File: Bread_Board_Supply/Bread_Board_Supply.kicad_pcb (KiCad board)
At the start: 2 copper layers, 63 x 38.6 mm, 27 parts, among them J1 3.3_Connector, J2 5V_Connector, J3 12V_Connector, J4 Barrel_Jack_Switch, SW1 SW_Wuerth_450301014042, U1 TPS562202, U2 LP5907MFX-3.3

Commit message: Layout Changes
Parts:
- moved C1 8.39 mm to (141.4, 82.4)
- moved C8 8.20 mm to (114.1, 88.4), turned to 90 degrees
- moved BLM18AG102S1ND1 0.98 mm to (130.7, 80.5), turned to -90 degrees
- turned C9 to 90 degrees
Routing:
- net +3.3V: track 0.00 -> 25.6 mm
- net +5V: track 0.00 -> 8.50 mm
- net Net-(U1-VFB): track 0.00 -> 4.93 mm
- net Net-(U1-VBST): track 0.00 -> 4.72 mm, vias 0 -> 1
- net Net-(D3-A): track 0.00 -> 3.86 mm
- net Net-(D4-A): track 0.00 -> 2.58 mm
- net Net-(D2-A): track 0.00 -> 2.38 mm
- net Net-(U1-EN): track 0.00 -> 1.71 mm
- added copper zone on F.Cu, net +12V
- added copper zone on B.Cu, net GND
- added copper zone on F.Cu, net Net-(U1-EN)
- added copper zone on F.Cu, net Net-(U1-SW)

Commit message: Layout finished
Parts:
- moved R5 20.6 mm to (135.7, 93.1)
- moved BLM18AG102S1ND1 19.9 mm to (150.5, 79.4), turned to 90 degrees
- moved R4 15.1 mm to (123.0, 89.9)
- moved C7 14.2 mm to (133.6, 85.6)
- moved C2 8.70 mm to (140.2, 79.7)
- moved C9 6.05 mm to (114.1, 86.7), turned to 0 degrees
- moved C1 5.51 mm to (146.2, 79.7), turned to 90 degrees
- moved C6 4.86 mm to (127.8, 84.4)
- moved U1 4.77 mm to (126.4, 80.1)
- moved D2 4.65 mm to (132.8, 73.7)
- moved R3 4.65 mm to (149.1, 73.9)
- moved C8 4.14 mm to (114.1, 92.5)
- moved L1 3.99 mm to (122.3, 82.5)
- moved C10 2.74 mm to (134.4, 79.7), turned to 90 degrees
- moved J3 0.50 mm to (104.5, 101.5)
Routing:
- net +5V: track 8.50 -> 46.3 mm
- net +12V: track 0.00 -> 19.1 mm
- net Net-(U1-VFB): track 4.93 -> 17.9 mm
- net Net-(U1-SW): track 0.00 -> 9.10 mm
- net GND: track 0.00 -> 8.57 mm, vias 0 -> 1
- net Net-(U1-EN): track 1.71 -> 2.32 mm
- net Net-(U1-VBST): track 4.72 -> 4.76 mm, vias 1 -> 0
- added copper zone on F.Cu, net +5V
- added copper zone on F.Cu, net GND
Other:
- outline, holes or cut-outs redrawn
- board text added: "+"
- board text added: "-"
- board text added: "3.3V"
- board text added: "5V"
- board text added: "Bread_Board power supply 5V & 3.3V"

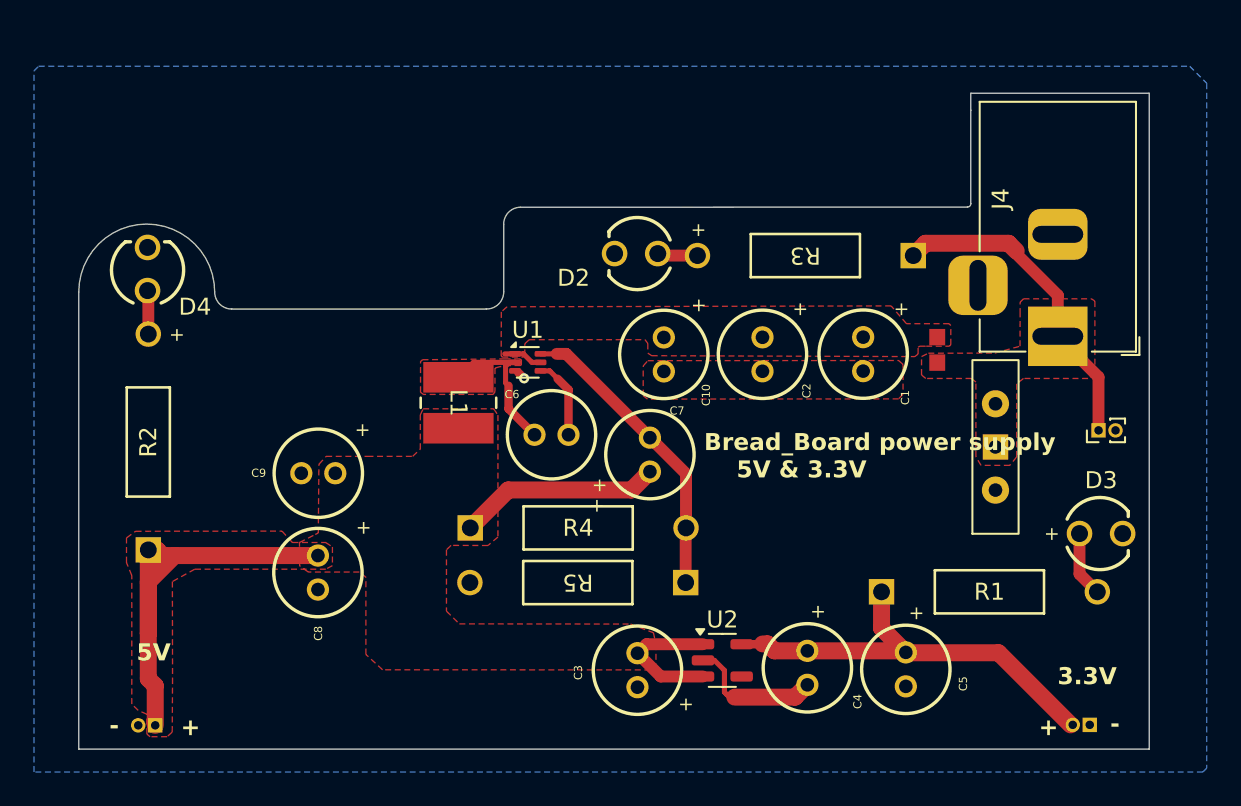
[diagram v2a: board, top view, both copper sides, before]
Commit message: USB C added
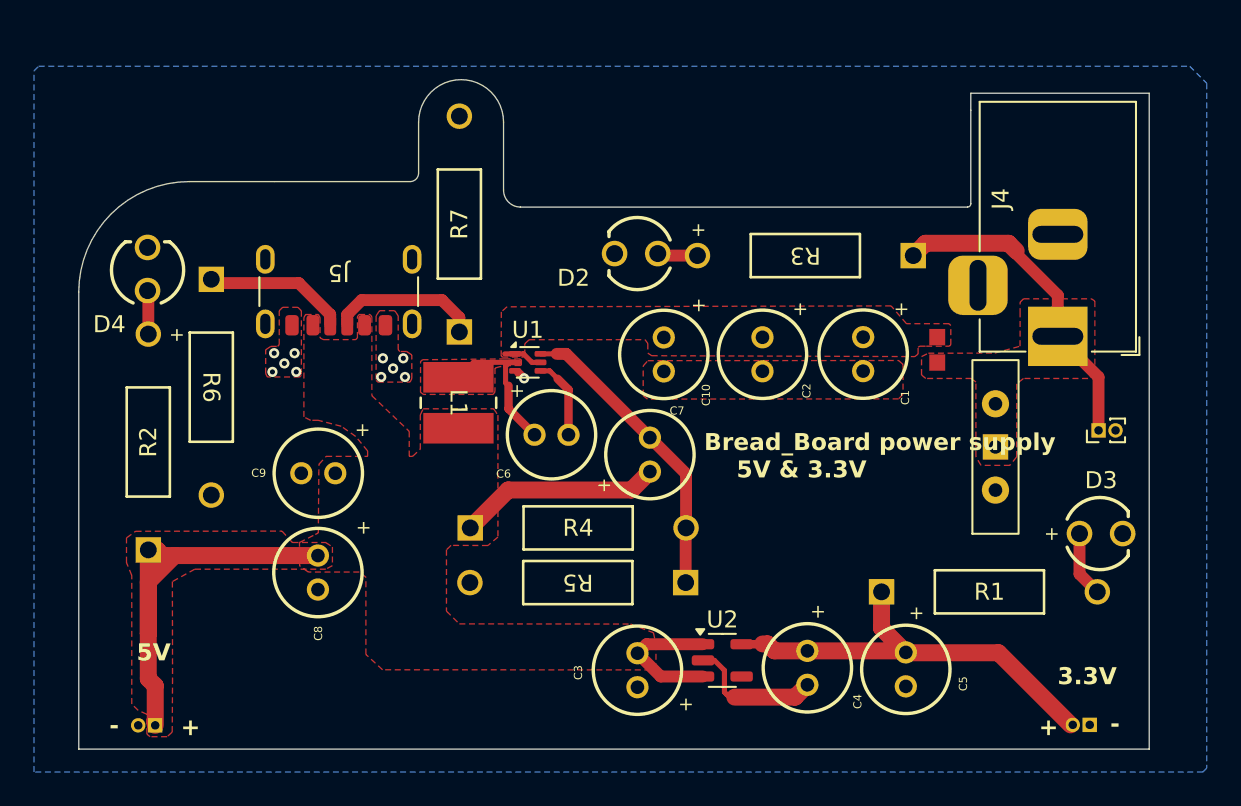
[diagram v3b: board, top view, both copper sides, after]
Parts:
- added J5: USB_C_Receptacle_PowerOnly_6P, Connector_USB:USB_C_Receptacle_GCT_USB4125-xx-x_6P_TopMnt_Horizontal, F.Cu at (115.3, 74.9)
- added R6: 5.1K, Bread_Board_powers:ERL07_VIS, F.Cu at (107.8, 75.2)
- added R7: 5.1K, Bread_Board_powers:ERL07_VIS, F.Cu at (122.4, 78.3)
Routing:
- net Net-(J5-CC1): track 0.00 -> 8.86 mm
- net Net-(J5-CC2): track 0.00 -> 8.49 mm
- net GND: vias 1 -> 11
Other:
- board size 63 x 38.6 mm -> 63 x 39.4 mm

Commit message: ground routing
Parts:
- moved C8 2.03 mm to (112.9, 90.8), turned to -90 degrees
- moved C1 1.65 mm to (146.2, 78.0)
- moved C2 1.65 mm to (140.2, 78.0)
- moved C3 1.65 mm to (132.9, 96.6), turned to -90 degrees
- moved C4 1.65 mm to (142.9, 96.5)
- moved C6 1.65 mm to (127.8, 82.8)
- moved C7 1.65 mm to (133.6, 83.9)
- moved C9 1.65 mm to (114.1, 85.0)
- moved D3 1.65 mm to (160.2, 88.6)
- moved J2 1.65 mm to (160.0, 82.5)
- moved J3 1.65 mm to (104.5, 99.8)
- moved J4 1.65 mm to (157.6, 77.0)
- moved J5 1.65 mm to (115.3, 73.2)
- moved L1 1.65 mm to (122.3, 80.9)
- moved R1 1.65 mm to (147.2, 92.0)
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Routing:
- net GND: track 8.57 -> 133.5 mm, vias 11 -> 12
- net +5V: track 46.3 -> 42.4 mm
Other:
- board size 63 x 39.4 mm -> 63 x 38.8 mm
